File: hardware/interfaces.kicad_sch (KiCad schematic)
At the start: 5 parts, among them J3 SSQ-126-04-G-D, J4 SSQ-126-04-G-D, J5 FFC_HDGC_1x22_0.5K-DX-22PWB

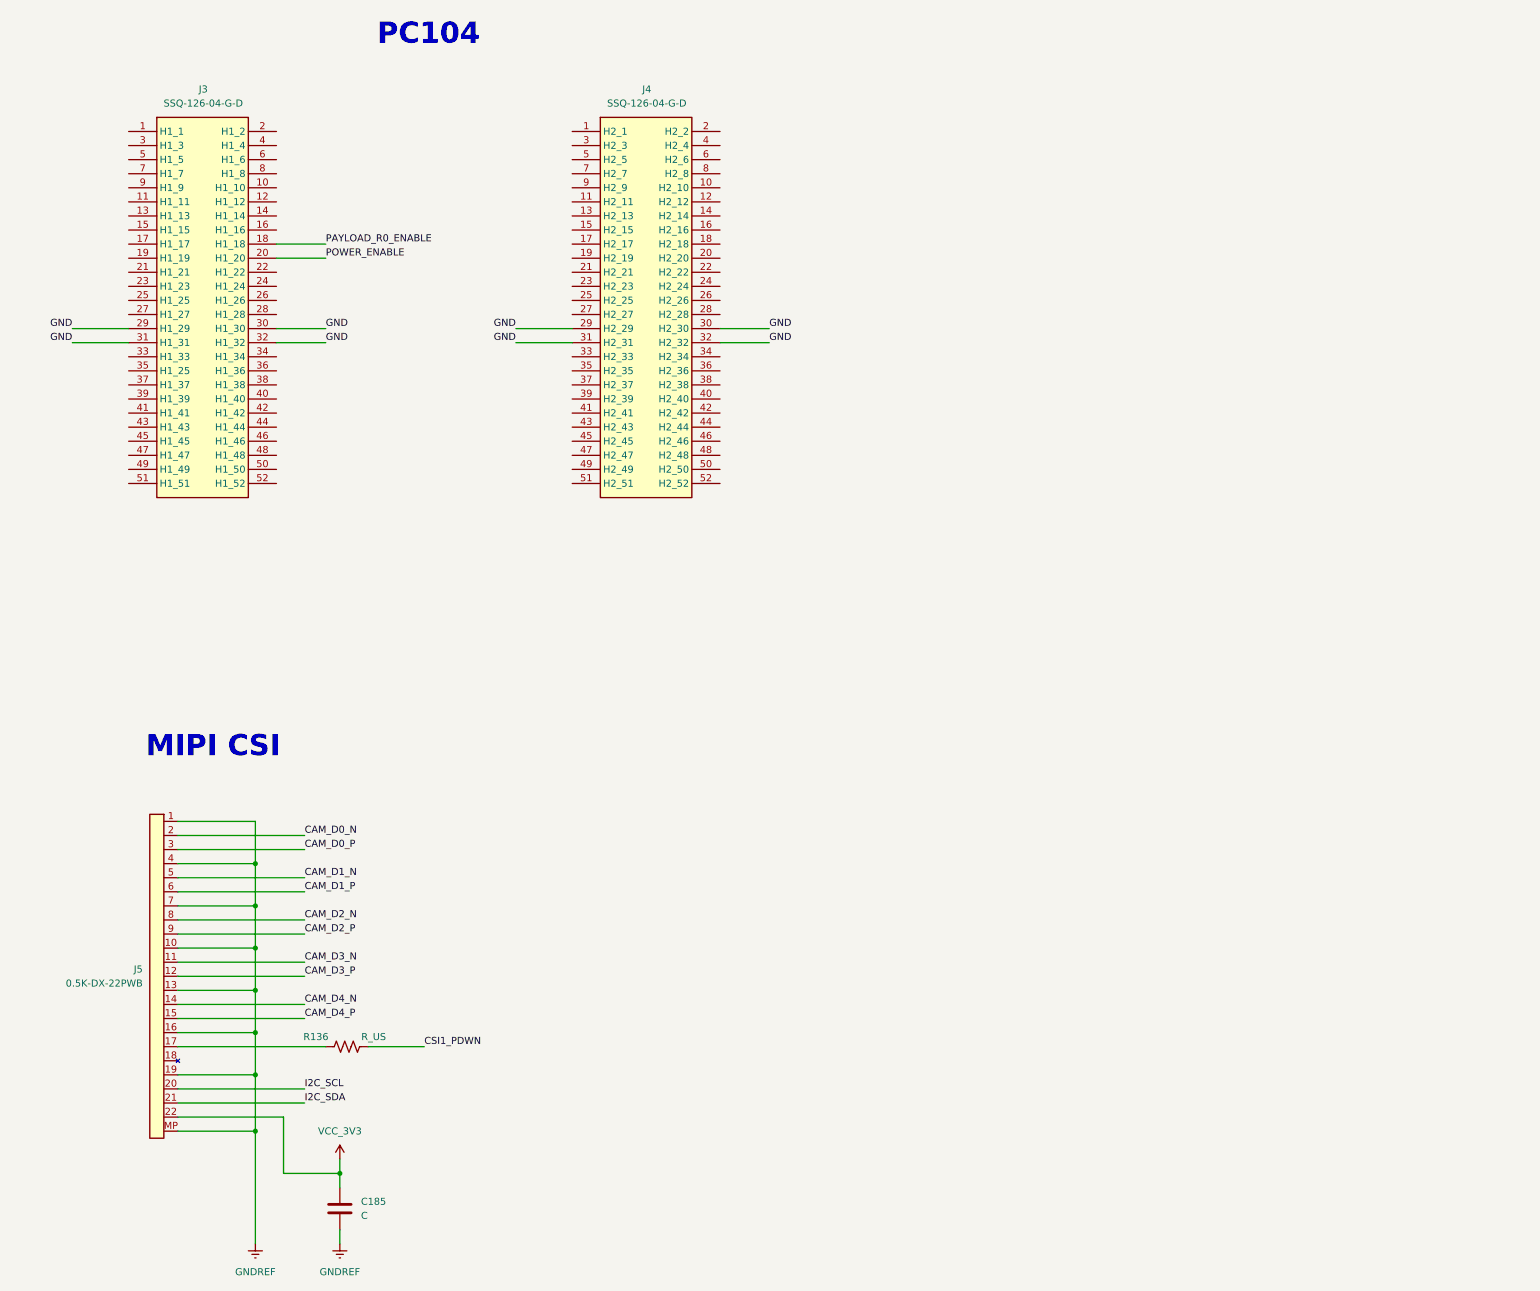
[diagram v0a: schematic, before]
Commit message: need review of MAX2771 connections, LDOs in general, names for the PC104 pins and his connection to other devices, include or exclude devices
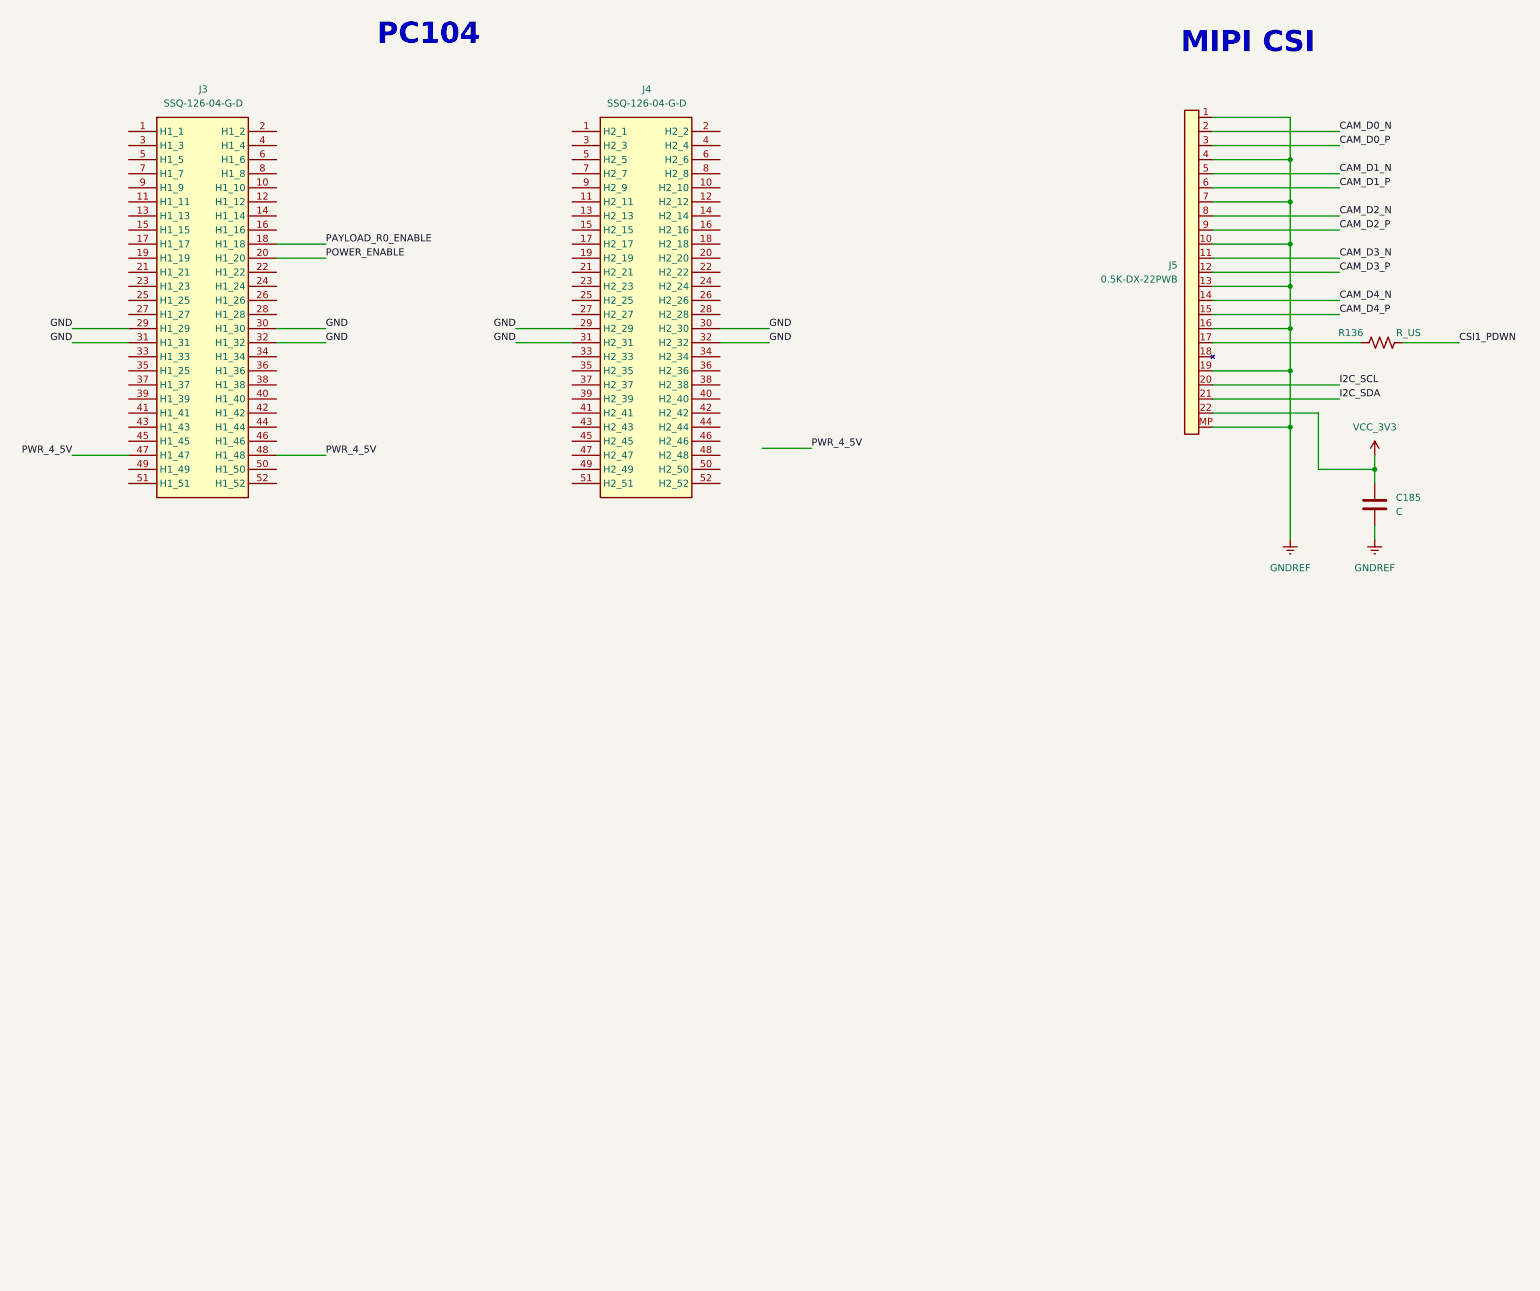
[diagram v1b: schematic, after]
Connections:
- net PWR_4_5V: now reaches J3.47 (H1_47)
- net PWR_4_5V: now also J3.48 (H1_48)
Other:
- moved on the sheet: C185, J5, R136
